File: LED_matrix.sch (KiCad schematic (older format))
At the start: 81 parts, among them J1 Conn_02x20_Odd_Even

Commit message: start adding more dense LED matrix
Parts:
- gave numbers to parts that had none: 4
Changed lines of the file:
@@
 NoConn ~ 3800 3200
 $Comp
-L Device:LED D?
+L Device:LED D61
 U 1 1 5C878379
 P 9400 1050
-F 0 "D?" V 9438 933 50  0000 R CNN
+F 0 "D61" V 9438 933 50  0000 R CNN
 F 1 "LED" V 9347 933 50  0000 R CNN
 F 2 "custom_LED_footprint:LED_0402_1005Metric" H 9400 1050 50  0001 C CNN
@@
 $EndComp
 $Comp
-L Device:LED D?
+L Device:LED D63
 U 1 1 5C8786C5
 P 9800 1050
-F 0 "D?" V 9838 933 50  0000 R CNN
+F 0 "D63" V 9838 933 50  0000 R CNN
 F 1 "LED" V 9747 933 50  0000 R CNN
 F 2 "custom_LED_footprint:LED_0402_1005Metric" H 9800 1050 50  0001 C CNN
@@
 $EndComp
 $Comp
-L Device:LED D?
+L Device:LED D62
 U 1 1 5C878793
 P 9400 1500
-F 0 "D?" V 9438 1383 50  0000 R CNN
+F 0 "D62" V 9438 1383 50  0000 R CNN
 F 1 "LED" V 9347 1383 50  0000 R CNN
 F 2 "custom_LED_footprint:LED_0402_1005Metric" H 9400 1500 50  0001 C CNN
@@
 	9400 1750 9400 1650
 $Comp
-L Device:LED D?
+L Device:LED D64
 U 1 1 5C8D99F4
 P 9800 1500
-F 0 "D?" V 9838 1383 50  0000 R CNN
+F 0 "D64" V 9838 1383 50  0000 R CNN
 F 1 "LED" V 9747 1383 50  0000 R CNN
 F 2 "custom_LED_footprint:LED_0402_1005Metric" H 9800 1500 50  0001 C CNN

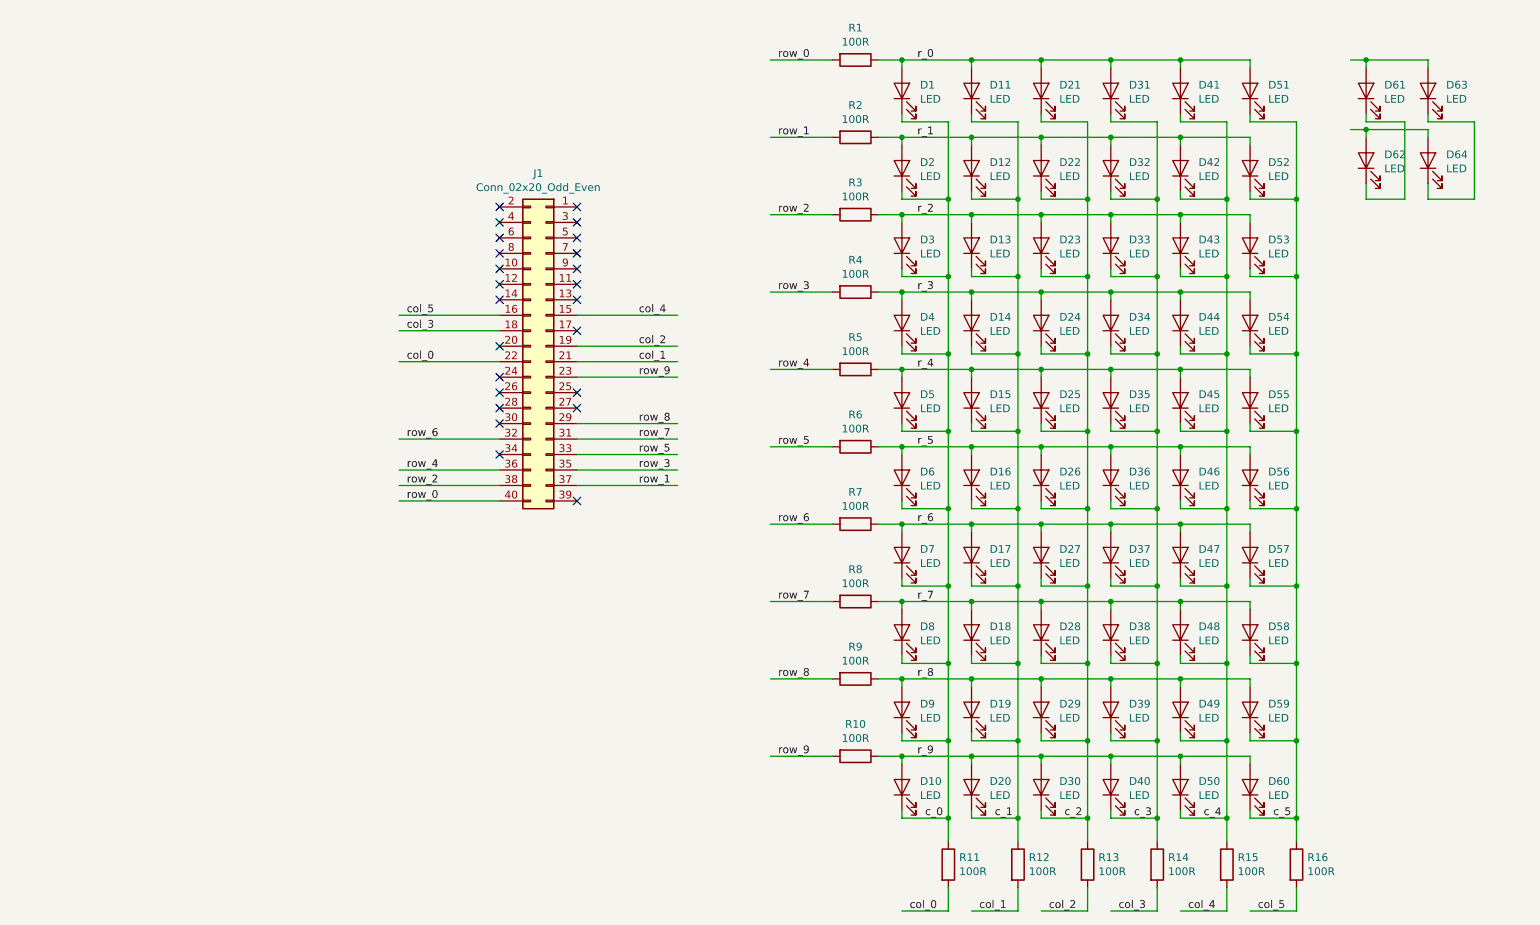
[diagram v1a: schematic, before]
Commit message: add LED matrix with 1.2mm pitch
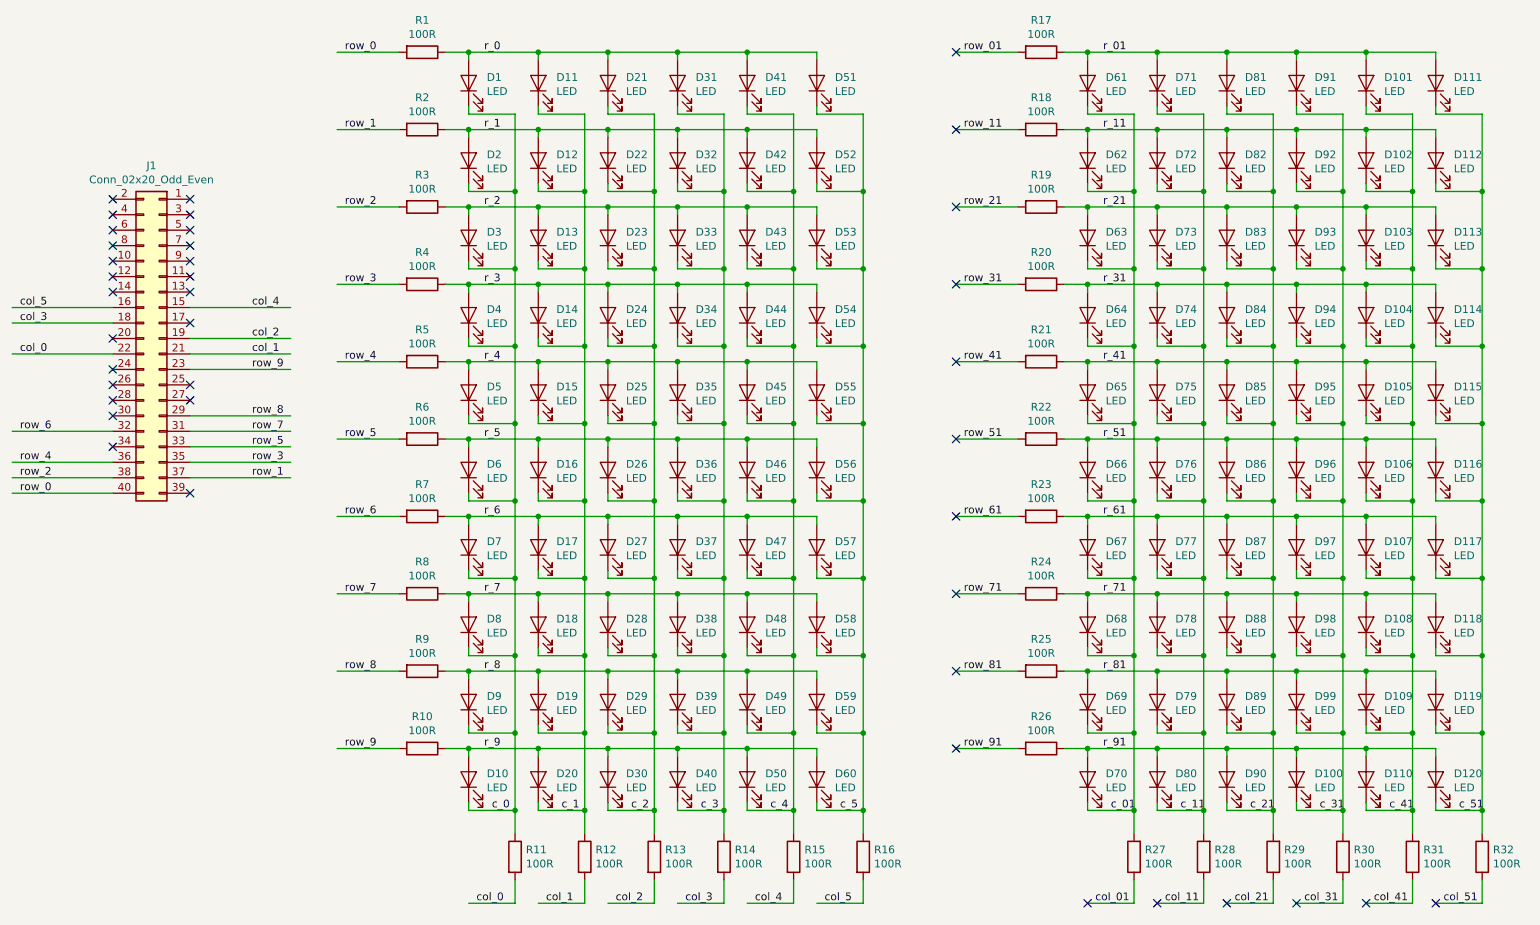
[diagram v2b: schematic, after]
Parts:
- added D100, D101, D102, D103, D104, D105, D106, D107, D108, D109, D110, D111, D112, D113, D114, D115, D116, D117, D118, D119, D120, D65, D66, D67, D68, D69, D70, D71, D72, D73, D74, D75, D76, D77, D78, D79, D80, D81, D82, D83, D84, D85, D86, D87, D88, D89, D90, D91, D92, D93, D94, D95, D96, D97, D98, D99: LED, custom_LED_footprint:LED_0402_round, symbol Device:LED
- added R17, R18, R19, R20, R21, R22, R23, R24, R25, R26, R27, R28, R29, R30, R31, R32: 100R, Resistors_SMD:R_0603, symbol Device:R
- D61, D62, D63, D64: footprint custom_LED_footprint:LED_0402_1005Metric -> custom_LED_footprint:LED_0402_round
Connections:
- net labels added: c_01, c_11, c_21, c_31, c_41, c_51, col_01, col_11, col_21, col_31, col_41, col_51, r_01, r_11, r_21, r_31, r_41, r_51, r_61, r_71, r_81, r_91, row_01, row_11, row_21, row_31, row_41, row_51, row_61, row_71, row_81, row_91
- wire segments 356 -> 660
- no-connect marks 24 -> 40
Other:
- moved on the sheet: D1, D10, D11, D12, D13, D14, D15, D16, D17, D18, D19, D2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

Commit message: move to 0.2/0.5 vias
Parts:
- R17, R18, R19, R20, R21, R22, R23, R24, R25, R26, R27, R28, R29, R30, R31, R32: footprint Resistors_SMD:R_0603 -> Resistor_SMD:R_0603_1608Metric
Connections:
- net labels removed: col_01, col_11, col_21, col_31, col_41, col_51, row_01, row_11, row_21, row_31, row_41, row_51, row_61, row_71, row_81, row_91
- no-connect marks 40 -> 24
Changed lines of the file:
@@
 	10150 6300 9850 6300
 Text Label 6800 800  0    50   ~ 0
-row_01
+row_0
 Text Label 6800 1300 0    50   ~ 0
-row_11
+row_1
 Text Label 6800 1800 0    50   ~ 0
-row_21
+row_2
 Text Label 6800 2300 0    50   ~ 0
-row_31
+row_3
 Text Label 6800 2800 0    50   ~ 0
-row_41
+row_4
 Text Label 6800 3300 0    50   ~ 0
-row_51
+row_5
 Text Label 6800 3800 0    50   ~ 0
-row_61
+row_6
 Text Label 6800 4300 0    50   ~ 0
-row_71
+row_7
 Text Label 6800 4800 0    50   ~ 0
-row_81
+row_8
 Text Label 6800 5300 0    50   ~ 0
-row_91
+row_9
 Text Label 7650 6300 0    50   ~ 0
-col_01
+col_0
 Text Label 8100 6300 0    50   ~ 0
-col_11
+col_1
 Text Label 8550 6300 0    50   ~ 0
-col_21
+col_2
 Text Label 9000 6300 0    50   ~ 0
-col_31
+col_3
 Text Label 9450 6300 0    50   ~ 0
-col_41
+col_4
 Text Label 9900 6300 0    50   ~ 0
-col_51
+col_5
 Text Label 7700 800  0    50   ~ 0
 r_01
@@
 Connection ~ 8350 3700
 Connection ~ 8350 4200
-NoConn ~ 6750 800
-NoConn ~ 6750 1300
-NoConn ~ 6750 1800
-NoConn ~ 6750 2300
-NoConn ~ 6750 2800
-NoConn ~ 6750 3300
-NoConn ~ 6750 3800
-NoConn ~ 6750 4300
-NoConn ~ 6750 4800
-NoConn ~ 6750 5300
-NoConn ~ 7600 6300
-NoConn ~ 8050 6300
-NoConn ~ 8500 6300
-NoConn ~ 8950 6300
-NoConn ~ 9400 6300
-NoConn ~ 9850 6300
 $Comp
 L Device:R R17
@@
 F 0 "R17" V 7093 800 50  0000 C CNN
 F 1 "100R" V 7184 800 50  0000 C CNN
-F 2 "Resistors_SMD:R_0603" V 7230 800 50  0001 C CNN
+F 2 "Resistor_SMD:R_0603_1608Metric" V 7230 800 50  0001 C CNN
 F 3 "~" H 7300 800 50  0001 C CNN
 	1    7300 800
@@
 F 0 "R18" V 7093 1300 50  0000 C CNN
 F 1 "100R" V 7184 1300 50  0000 C CNN
-F 2 "Resistors_SMD:R_0603" V 7230 1300 50  0001 C CNN
+F 2 "Resistor_SMD:R_0603_1608Metric" V 7230 1300 50  0001 C CNN
 F 3 "~" H 7300 1300 50  0001 C CNN
 	1    7300 1300
@@
 F 0 "R19" V 7093 1800 50  0000 C CNN
 F 1 "100R" V 7184 1800 50  0000 C CNN
-F 2 "Resistors_SMD:R_0603" V 7230 1800 50  0001 C CNN
+F 2 "Resistor_SMD:R_0603_1608Metric" V 7230 1800 50  0001 C CNN
 F 3 "~" H 7300 1800 50  0001 C CNN
 	1    7300 1800
@@
 F 0 "R20" V 7093 2300 50  0000 C CNN
 F 1 "100R" V 7184 2300 50  0000 C CNN
-F 2 "Resistors_SMD:R_0603" V 7230 2300 50  0001 C CNN
+F 2 "Resistor_SMD:R_0603_1608Metric" V 7230 2300 50  0001 C CNN
 F 3 "~" H 7300 2300 50  0001 C CNN
 	1    7300 2300
@@
 F 0 "R21" V 7093 2800 50  0000 C CNN
 F 1 "100R" V 7184 2800 50  0000 C CNN
-F 2 "Resistors_SMD:R_0603" V 7230 2800 50  0001 C CNN
+F 2 "Resistor_SMD:R_0603_1608Metric" V 7230 2800 50  0001 C CNN
 F 3 "~" H 7300 2800 50  0001 C CNN
 	1    7300 2800
@@
 F 0 "R22" V 7093 3300 50  0000 C CNN
 F 1 "100R" V 7184 3300 50  0000 C CNN
-F 2 "Resistors_SMD:R_0603" V 7230 3300 50  0001 C CNN
+F 2 "Resistor_SMD:R_0603_1608Metric" V 7230 3300 50  0001 C CNN
 F 3 "~" H 7300 3300 50  0001 C CNN
 	1    7300 3300
@@
 F 0 "R23" V 7093 3800 50  0000 C CNN
 F 1 "100R" V 7184 3800 50  0000 C CNN
-F 2 "Resistors_SMD:R_0603" V 7230 3800 50  0001 C CNN
+F 2 "Resistor_SMD:R_0603_1608Metric" V 7230 3800 50  0001 C CNN
 F 3 "~" H 7300 3800 50  0001 C CNN
 	1    7300 3800
@@
 F 0 "R24" V 7093 4300 50  0000 C CNN
 F 1 "100R" V 7184 4300 50  0000 C CNN
-F 2 "Resistors_SMD:R_0603" V 7230 4300 50  0001 C CNN
+F 2 "Resistor_SMD:R_0603_1608Metric" V 7230 4300 50  0001 C CNN
 F 3 "~" H 7300 4300 50  0001 C CNN
 	1    7300 4300
@@
 F 0 "R25" V 7093 4800 50  0000 C CNN
 F 1 "100R" V 7184 4800 50  0000 C CNN
-F 2 "Resistors_SMD:R_0603" V 7230 4800 50  0001 C CNN
+F 2 "Resistor_SMD:R_0603_1608Metric" V 7230 4800 50  0001 C CNN
 F 3 "~" H 7300 4800 50  0001 C CNN
 	1    7300 4800
@@
 F 0 "R26" V 7093 5300 50  0000 C CNN
 F 1 "100R" V 7184 5300 50  0000 C CNN
-F 2 "Resistors_SMD:R_0603" V 7230 5300 50  0001 C CNN
+F 2 "Resistor_SMD:R_0603_1608Metric" V 7230 5300 50  0001 C CNN
 F 3 "~" H 7300 5300 50  0001 C CNN
 	1    7300 5300
@@
 F 0 "R27" H 7830 5954 50  0000 R CNN
 F 1 "100R" H 7830 6045 50  0000 R CNN
-F 2 "Resistors_SMD:R_0603" V 7830 6000 50  0001 C CNN
+F 2 "Resistor_SMD:R_0603_1608Metric" V 7830 6000 50  0001 C CNN
 F 3 "~" H 7900 6000 50  0001 C CNN
 	1    7900 6000
@@
 F 0 "R28" H 8280 5954 50  0000 R CNN
 F 1 "100R" H 8280 6045 50  0000 R CNN
-F 2 "Resistors_SMD:R_0603" V 8280 6000 50  0001 C CNN
+F 2 "Resistor_SMD:R_0603_1608Metric" V 8280 6000 50  0001 C CNN
 F 3 "~" H 8350 6000 50  0001 C CNN
 	1    8350 6000
@@
 F 0 "R29" H 8730 5954 50  0000 R CNN
 F 1 "100R" H 8730 6045 50  0000 R CNN
-F 2 "Resistors_SMD:R_0603" V 8730 6000 50  0001 C CNN
+F 2 "Resistor_SMD:R_0603_1608Metric" V 8730 6000 50  0001 C CNN
 F 3 "~" H 8800 6000 50  0001 C CNN
 	1    8800 6000
@@
 F 0 "R30" H 9180 5954 50  0000 R CNN
 F 1 "100R" H 9180 6045 50  0000 R CNN
-F 2 "Resistors_SMD:R_0603" V 9180 6000 50  0001 C CNN
+F 2 "Resistor_SMD:R_0603_1608Metric" V 9180 6000 50  0001 C CNN
 F 3 "~" H 9250 6000 50  0001 C CNN
 	1    9250 6000
@@
 F 0 "R31" H 9630 5954 50  0000 R CNN
 F 1 "100R" H 9630 6045 50  0000 R CNN
-F 2 "Resistors_SMD:R_0603" V 9630 6000 50  0001 C CNN
+F 2 "Resistor_SMD:R_0603_1608Metric" V 9630 6000 50  0001 C CNN
 F 3 "~" H 9700 6000 50  0001 C CNN
 	1    9700 6000
@@
 F 0 "R32" H 10080 5954 50  0000 R CNN
 F 1 "100R" H 10080 6045 50  0000 R CNN
-F 2 "Resistors_SMD:R_0603" V 10080 6000 50  0001 C CNN
+F 2 "Resistor_SMD:R_0603_1608Metric" V 10080 6000 50  0001 C CNN
 F 3 "~" H 10150 6000 50  0001 C CNN
 	1    10150 6000
